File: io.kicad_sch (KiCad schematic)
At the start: 3 parts, among them J3 Conn_01x38, J4 Conn_01x22, J5 Conn_02x11

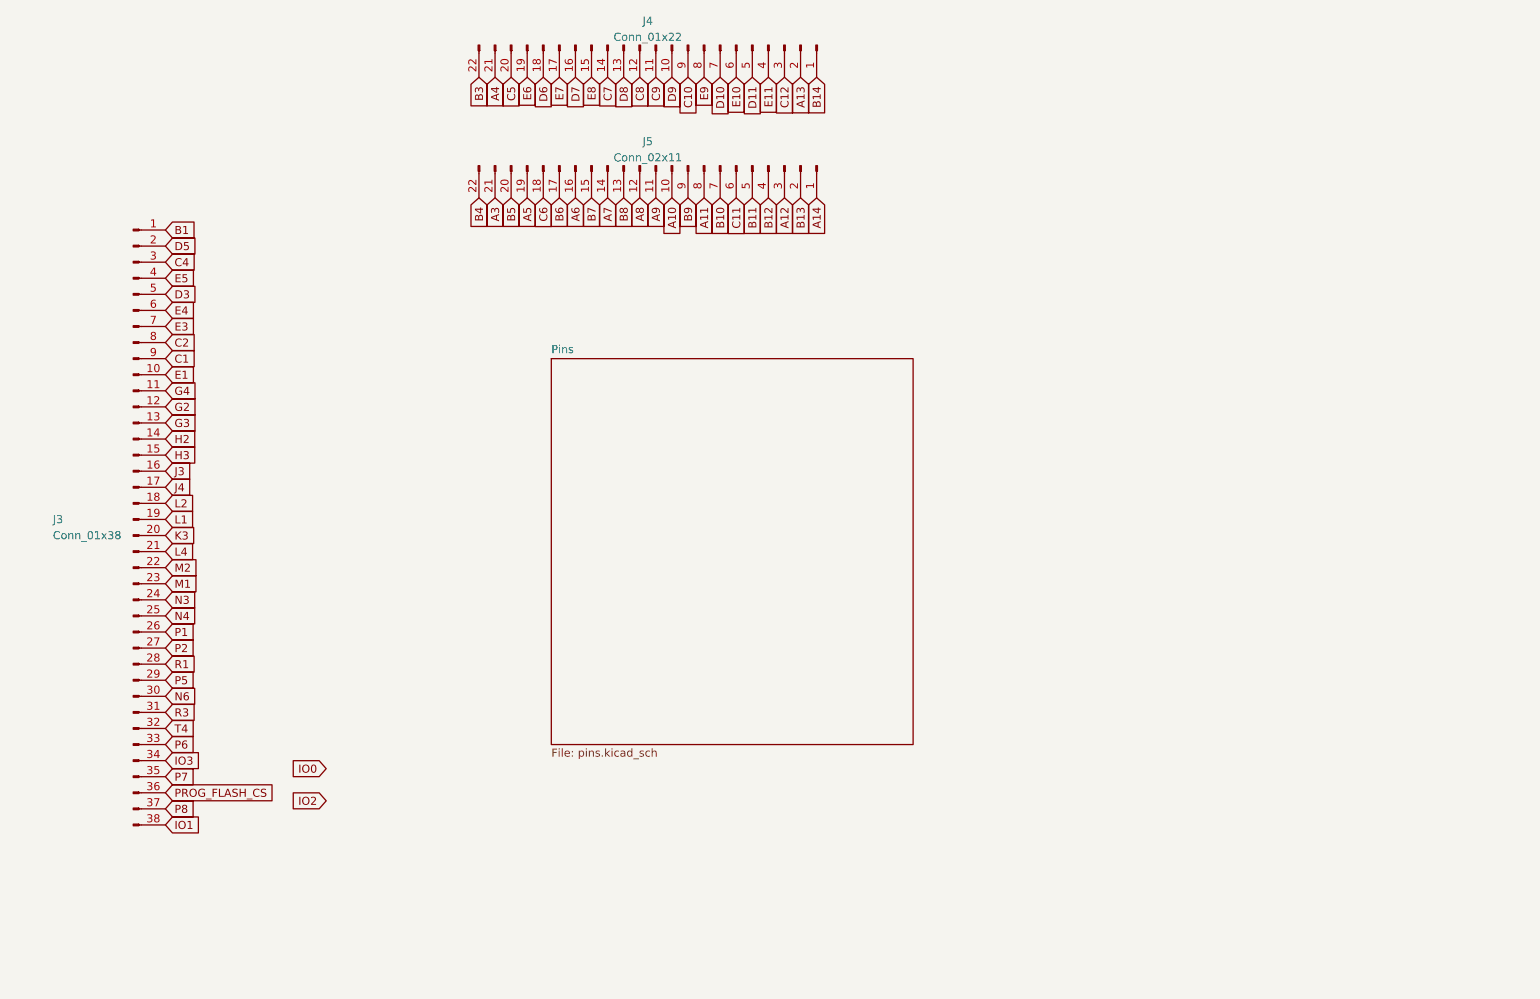
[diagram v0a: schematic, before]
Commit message: Small routing tweaks, add breakout to schematic
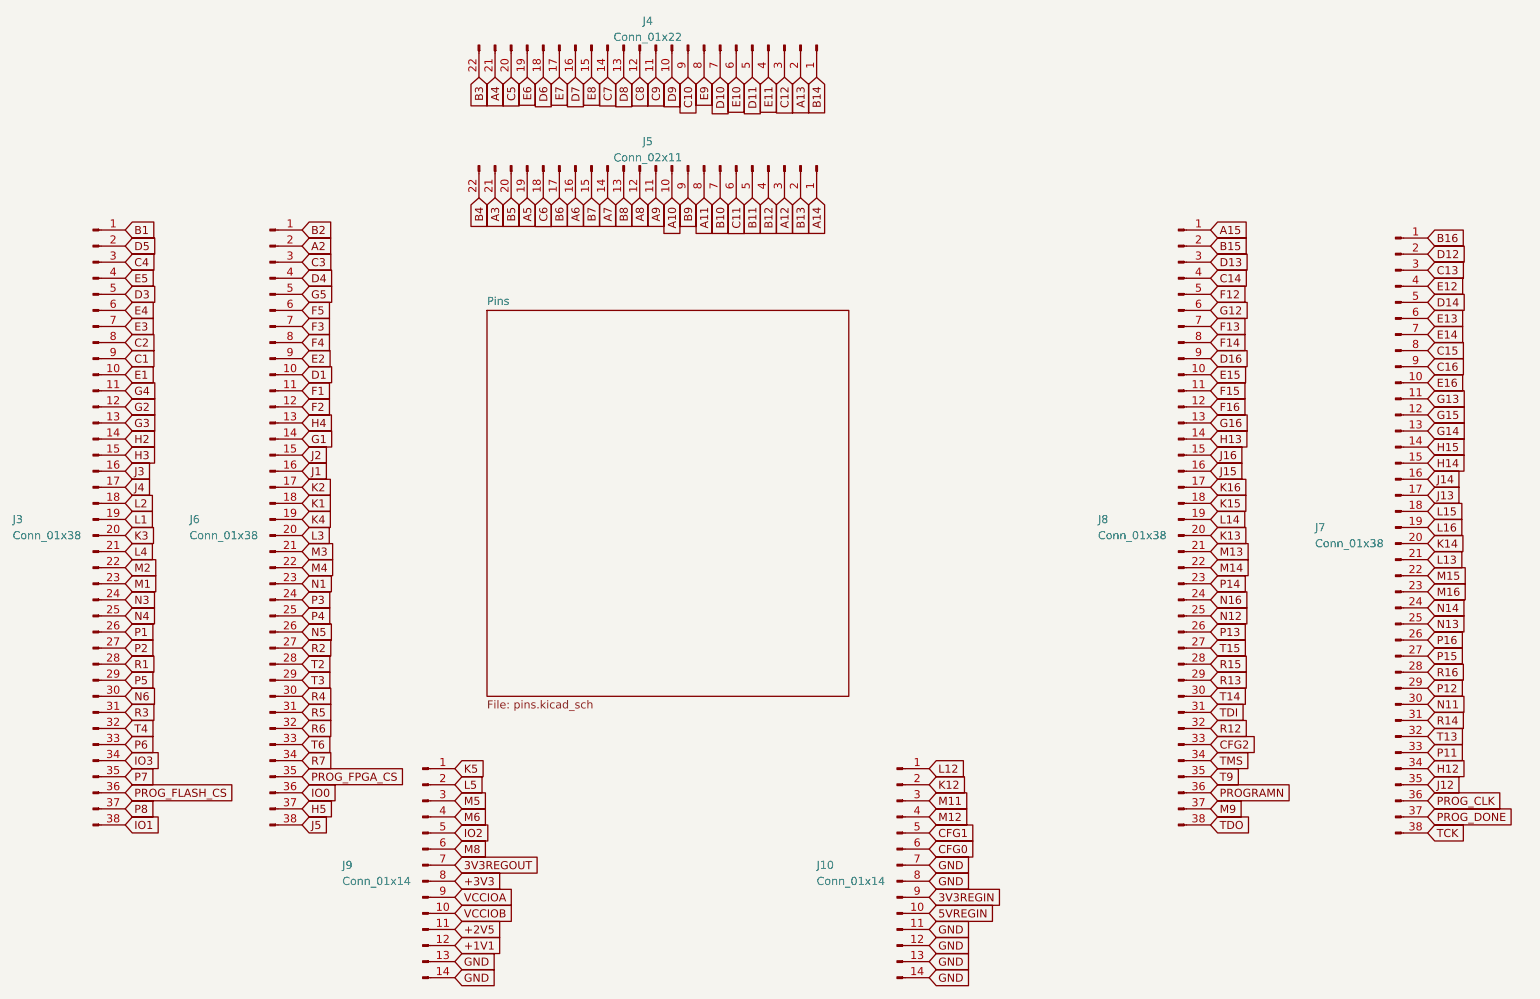
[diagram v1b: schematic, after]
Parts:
- added J10, J9: Conn_01x14, Connector_PinHeader_2.54mm:PinHeader_2x07_P2.54mm_Vertical, symbol Connector:Conn_01x14_Pin
- added J6, J8: Conn_01x38, Connector_PinHeader_2.54mm:PinHeader_2x19_P2.54mm_Vertical, symbol Connector:Conn_01x38_Pin
- added J7: Conn_01x38, Connector_PinHeader_1.27mm:PinHeader_1x38_P1.27mm_Vertical, symbol Connector:Conn_01x38_Pin
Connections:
- net IO0: now also J6.36 (Pin_36)
- net IO2: now also J9.5 (Pin_5)
- new net +1V1: J9.12 (Pin_12)
- new net +2V5: J9.11 (Pin_11)
- new net +3V3: J9.8 (Pin_8)
- new net 3V3REGIN: J10.9 (Pin_9)
- new net 3V3REGOUT: J9.7 (Pin_7)
- new net 5VREGIN: J10.10 (Pin_10)
- new net A15: J8.1 (Pin_1)
- new net A2: J6.2 (Pin_2)
- new net B15: J8.2 (Pin_2)
- new net B16: J7.1 (Pin_1)
- new net B2: J6.1 (Pin_1)
- new net C13: J7.3 (Pin_3)
- new net C14: J8.4 (Pin_4)
- new net C15: J7.8 (Pin_8)
- new net C16: J7.9 (Pin_9)
- new net C3: J6.3 (Pin_3)
- new net CFG0: J10.6 (Pin_6)
- new net CFG1: J10.5 (Pin_5)
- new net CFG2: J8.33 (Pin_33)
- new net D1: J6.10 (Pin_10)
- new net D12: J7.2 (Pin_2)
- new net D13: J8.3 (Pin_3)
- new net D14: J7.5 (Pin_5)
- new net D16: J8.9 (Pin_9)
- new net D4: J6.4 (Pin_4)
- new net E12: J7.4 (Pin_4)
- new net E13: J7.6 (Pin_6)
- new net E14: J7.7 (Pin_7)
- new net E15: J8.10 (Pin_10)
- new net E16: J7.10 (Pin_10)
- new net E2: J6.9 (Pin_9)
- new net F1: J6.11 (Pin_11)
- new net F12: J8.5 (Pin_5)
- new net F13: J8.7 (Pin_7)
- new net F14: J8.8 (Pin_8)
- new net F15: J8.11 (Pin_11)
- new net F16: J8.12 (Pin_12)
- new net F2: J6.12 (Pin_12)
- new net F3: J6.7 (Pin_7)
- new net F4: J6.8 (Pin_8)
- new net F5: J6.6 (Pin_6)
- new net G1: J6.14 (Pin_14)
- new net G12: J8.6 (Pin_6)
- new net G13: J7.11 (Pin_11)
- new net G14: J7.13 (Pin_13)
- new net G15: J7.12 (Pin_12)
- new net G16: J8.13 (Pin_13)
- new net G5: J6.5 (Pin_5)
- new net GND: J10.11 (Pin_11), J10.12 (Pin_12), J10.13 (Pin_13), J10.14 (Pin_14), J10.7 (Pin_7), J10.8 (Pin_8), J9.13 (Pin_13), J9.14 (Pin_14)
- new net H12: J7.34 (Pin_34)
- new net H13: J8.14 (Pin_14)
- new net H14: J7.15 (Pin_15)
- new net H15: J7.14 (Pin_14)
- new net H4: J6.13 (Pin_13)
- new net H5: J6.37 (Pin_37)
- new net J1: J6.16 (Pin_16)
- new net J12: J7.35 (Pin_35)
- new net J13: J7.17 (Pin_17)
- new net J14: J7.16 (Pin_16)
- new net J15: J8.16 (Pin_16)
- new net J16: J8.15 (Pin_15)
- new net J2: J6.15 (Pin_15)
- new net J5: J6.38 (Pin_38)
- new net K1: J6.18 (Pin_18)
- new net K12: J10.2 (Pin_2)
- new net K13: J8.20 (Pin_20)
- new net K14: J7.20 (Pin_20)
- new net K15: J8.18 (Pin_18)
- new net K16: J8.17 (Pin_17)
- new net K2: J6.17 (Pin_17)
- new net K4: J6.19 (Pin_19)
- new net K5: J9.1 (Pin_1)
- new net L12: J10.1 (Pin_1)
- new net L13: J7.21 (Pin_21)
- new net L14: J8.19 (Pin_19)
- new net L15: J7.18 (Pin_18)
- new net L16: J7.19 (Pin_19)
- new net L3: J6.20 (Pin_20)
- new net L5: J9.2 (Pin_2)
- new net M11: J10.3 (Pin_3)
- new net M12: J10.4 (Pin_4)
- new net M13: J8.21 (Pin_21)
- new net M14: J8.22 (Pin_22)
- new net M15: J7.22 (Pin_22)
- new net M16: J7.23 (Pin_23)
- new net M3: J6.21 (Pin_21)
- new net M4: J6.22 (Pin_22)
- new net M5: J9.3 (Pin_3)
- new net M6: J9.4 (Pin_4)
- new net M8: J9.6 (Pin_6)
- new net M9: J8.37 (Pin_37)
- new net N1: J6.23 (Pin_23)
- new net N11: J7.30 (Pin_30)
- new net N12: J8.25 (Pin_25)
- new net N13: J7.25 (Pin_25)
- new net N14: J7.24 (Pin_24)
- new net N16: J8.24 (Pin_24)
- new net N5: J6.26 (Pin_26)
- new net P11: J7.33 (Pin_33)
- new net P12: J7.29 (Pin_29)
- new net P13: J8.26 (Pin_26)
- new net P14: J8.23 (Pin_23)
- new net P15: J7.27 (Pin_27)
- new net P16: J7.26 (Pin_26)
- new net P3: J6.24 (Pin_24)
- new net P4: J6.25 (Pin_25)
- new net PROGRAMN: J8.36 (Pin_36)
- new net PROG_CLK: J7.36 (Pin_36)
- new net PROG_DONE: J7.37 (Pin_37)
- new net PROG_FPGA_CS: J6.35 (Pin_35)
- new net R12: J8.32 (Pin_32)
- new net R13: J8.29 (Pin_29)
- new net R14: J7.31 (Pin_31)
- new net R15: J8.28 (Pin_28)
- new net R16: J7.28 (Pin_28)
- new net R2: J6.27 (Pin_27)
- new net R4: J6.30 (Pin_30)
- new net R5: J6.31 (Pin_31)
- new net R6: J6.32 (Pin_32)
- new net R7: J6.34 (Pin_34)
- new net T13: J7.32 (Pin_32)
- new net T14: J8.30 (Pin_30)
- new net T15: J8.27 (Pin_27)
- new net T2: J6.28 (Pin_28)
- new net T3: J6.29 (Pin_29)
- new net T6: J6.33 (Pin_33)
- new net T9: J8.35 (Pin_35)
- new net TCK: J7.38 (Pin_38)
- new net TDI: J8.31 (Pin_31)
- new net TDO: J8.38 (Pin_38)
- new net TMS: J8.34 (Pin_34)
- new net VCCIOA: J9.9 (Pin_9)
- new net VCCIOB: J9.10 (Pin_10)
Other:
- moved on the sheet: J3

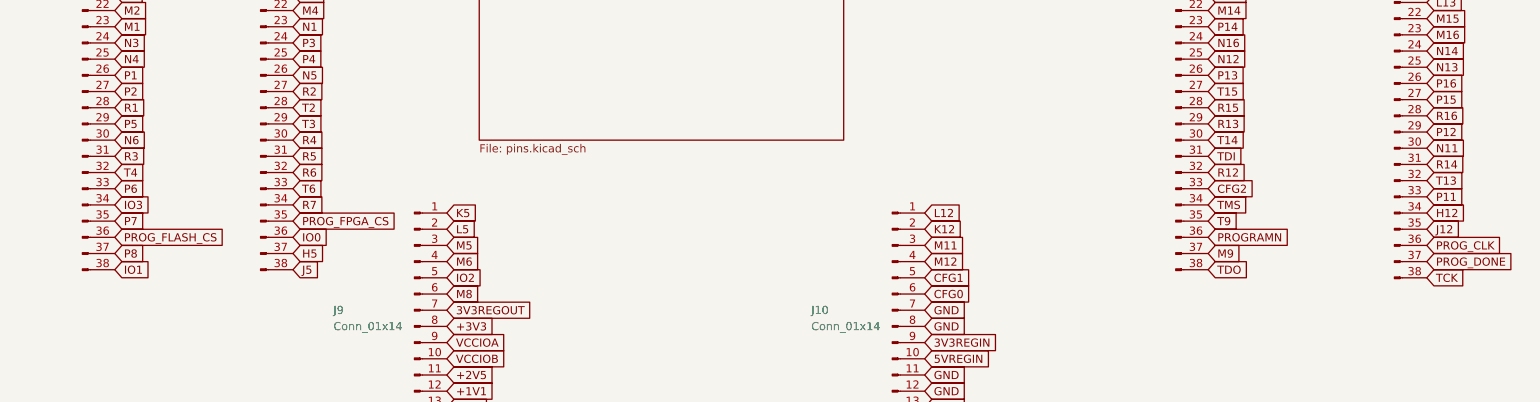
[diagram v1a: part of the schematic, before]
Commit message: Move programming pins to 100 mil headers
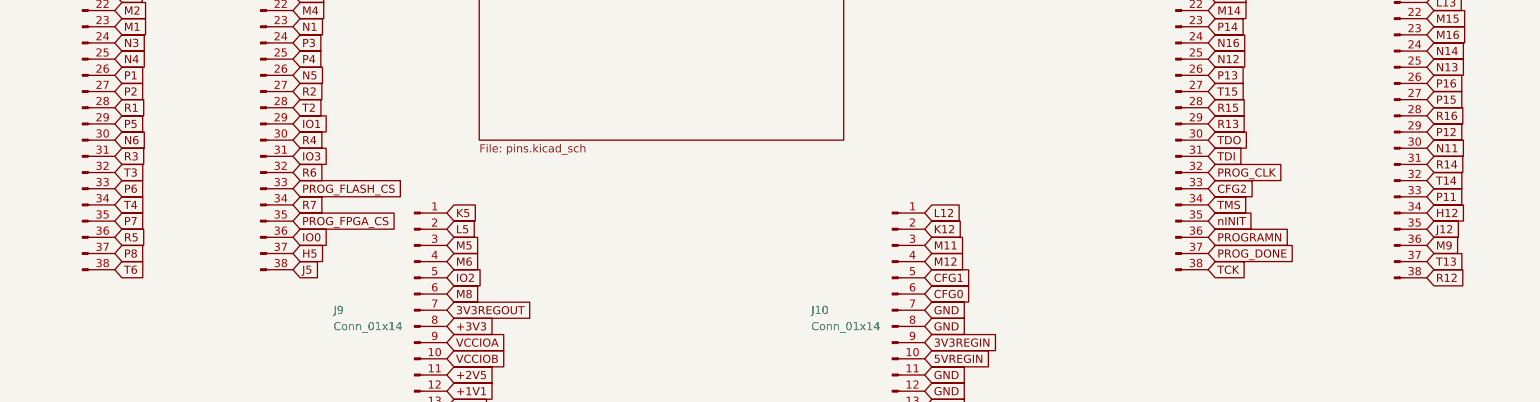
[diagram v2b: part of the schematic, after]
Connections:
- net IO1: now also J6.29 (Pin_29); no longer J3.38 (Pin_38)
- net IO3: now also J6.31 (Pin_31); no longer J3.34 (Pin_34)
- net M9: now also J7.36 (Pin_36); no longer J8.37 (Pin_37)
- net PROG_CLK: now also J8.32 (Pin_32); no longer J7.36 (Pin_36)
- net PROG_DONE: now also J8.37 (Pin_37); no longer J7.37 (Pin_37)
- net PROG_FLASH_CS: now also J6.33 (Pin_33); no longer J3.36 (Pin_36)
- net R12: now also J7.38 (Pin_38); no longer J8.32 (Pin_32)
- net R5: now also J3.36 (Pin_36); no longer J6.31 (Pin_31)
- net T13: now also J7.37 (Pin_37); no longer J7.32 (Pin_32)
- net T14: now also J7.32 (Pin_32); no longer J8.30 (Pin_30)
- net T3: now also J3.32 (Pin_32); no longer J6.29 (Pin_29)
- net T4: now also J3.34 (Pin_34); no longer J3.32 (Pin_32)
- net T6: now also J3.38 (Pin_38); no longer J6.33 (Pin_33)
- net TCK: now also J8.38 (Pin_38); no longer J7.38 (Pin_38)
- net TDO: now also J8.30 (Pin_30); no longer J8.38 (Pin_38)
- net T9 renamed nINIT

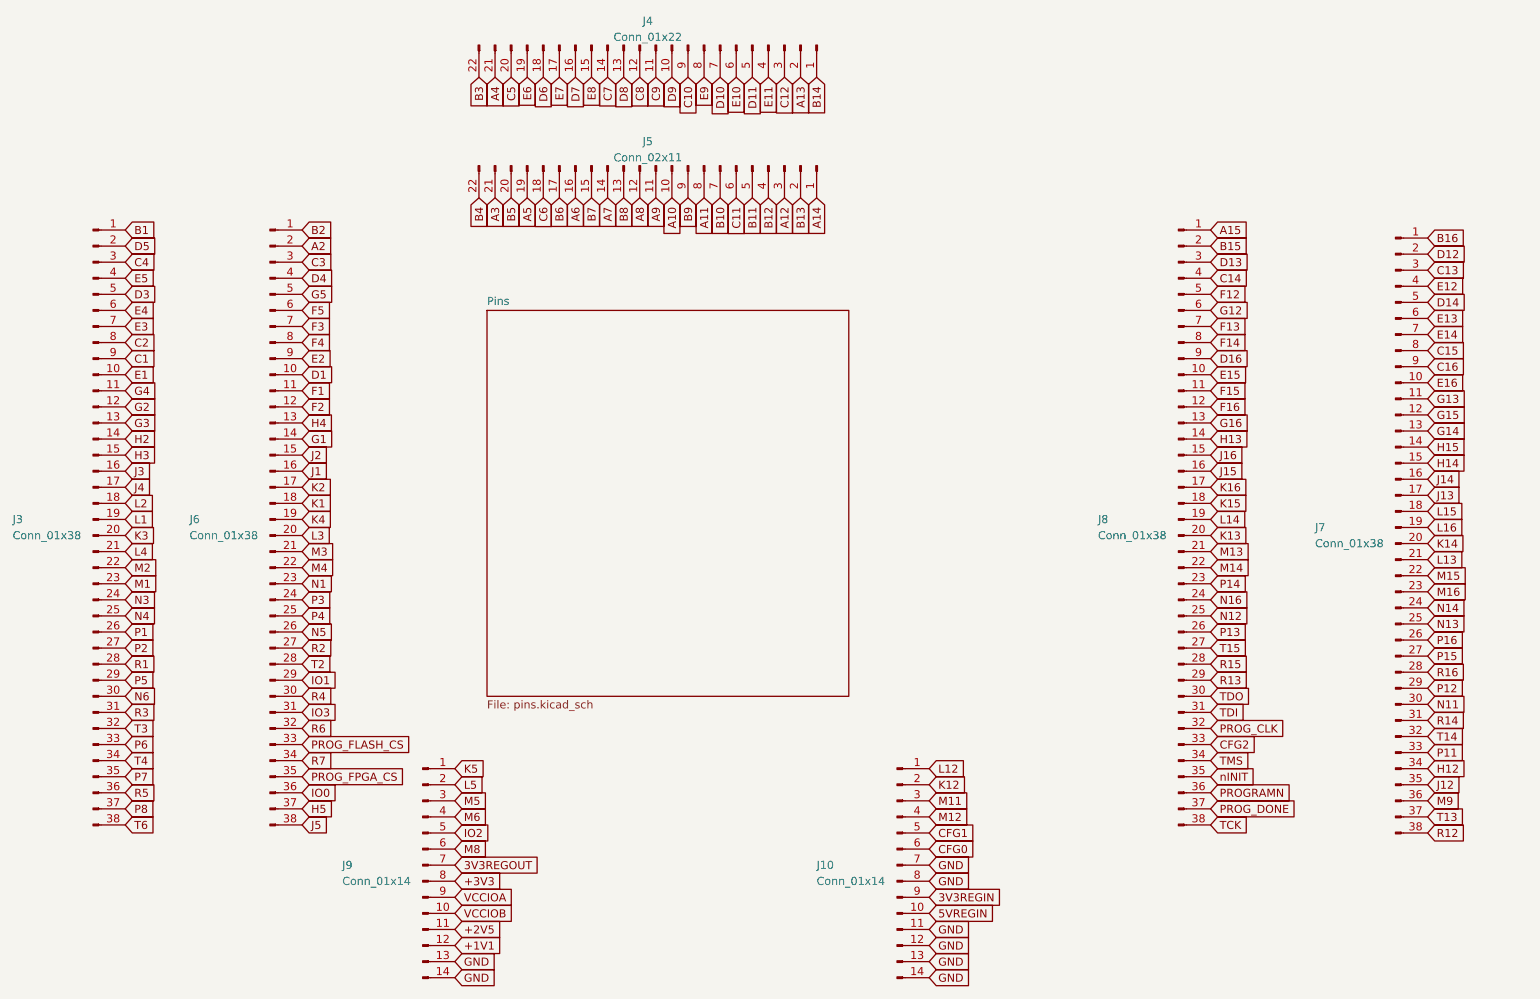
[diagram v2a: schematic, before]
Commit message: Schematic tweaks for readability
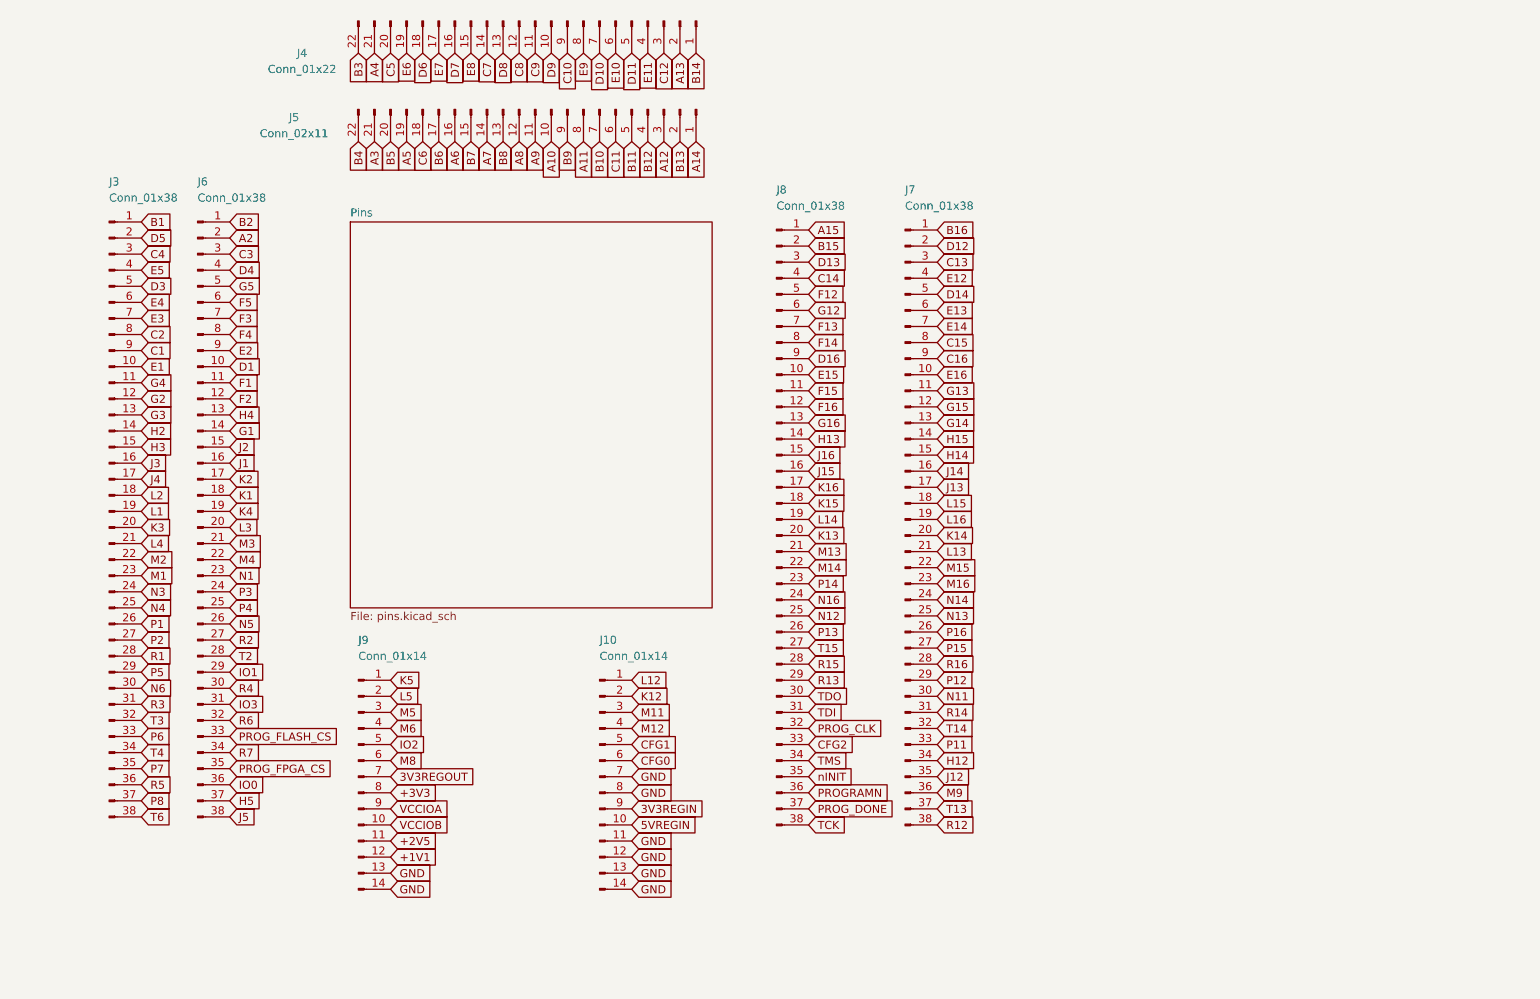
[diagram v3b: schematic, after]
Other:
- moved on the sheet: J10, J3, J4, J5, J6, J7, J8, J9
